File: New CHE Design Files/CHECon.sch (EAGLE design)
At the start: 42 parts, among them U2 MAX232SOIC16, U3 RS485SOIC

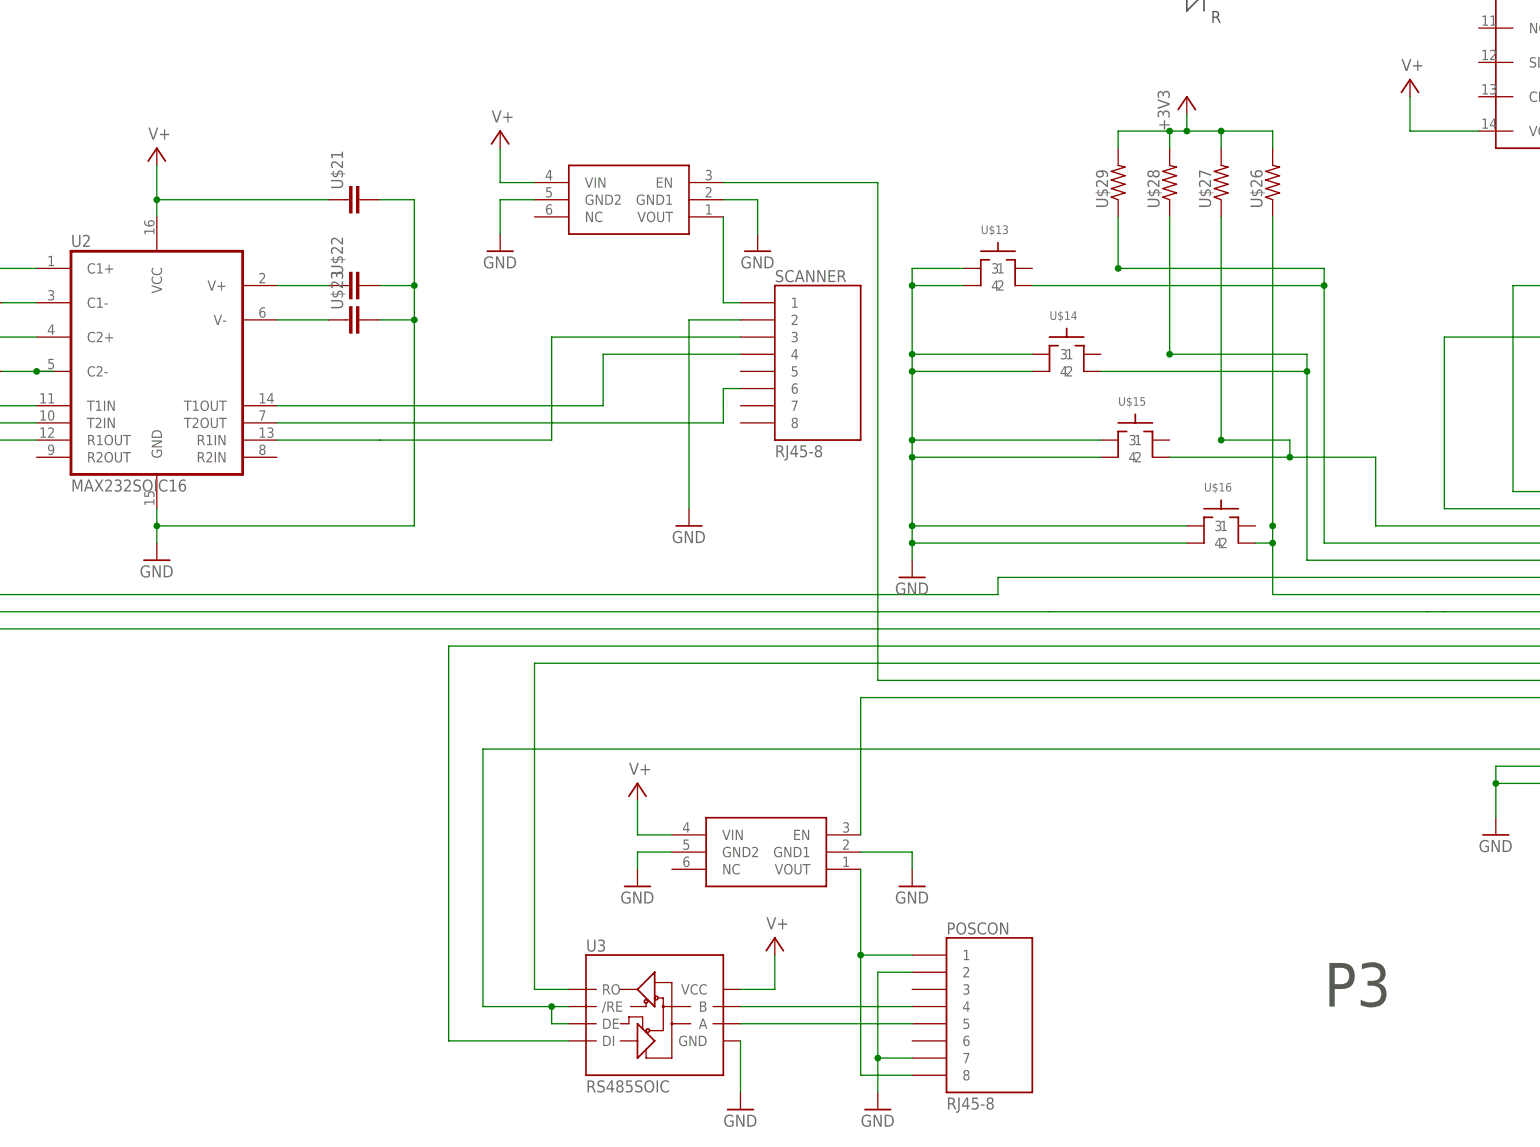
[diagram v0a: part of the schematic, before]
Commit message: P4
Fixed MAX232 rail, moved to 3.3V
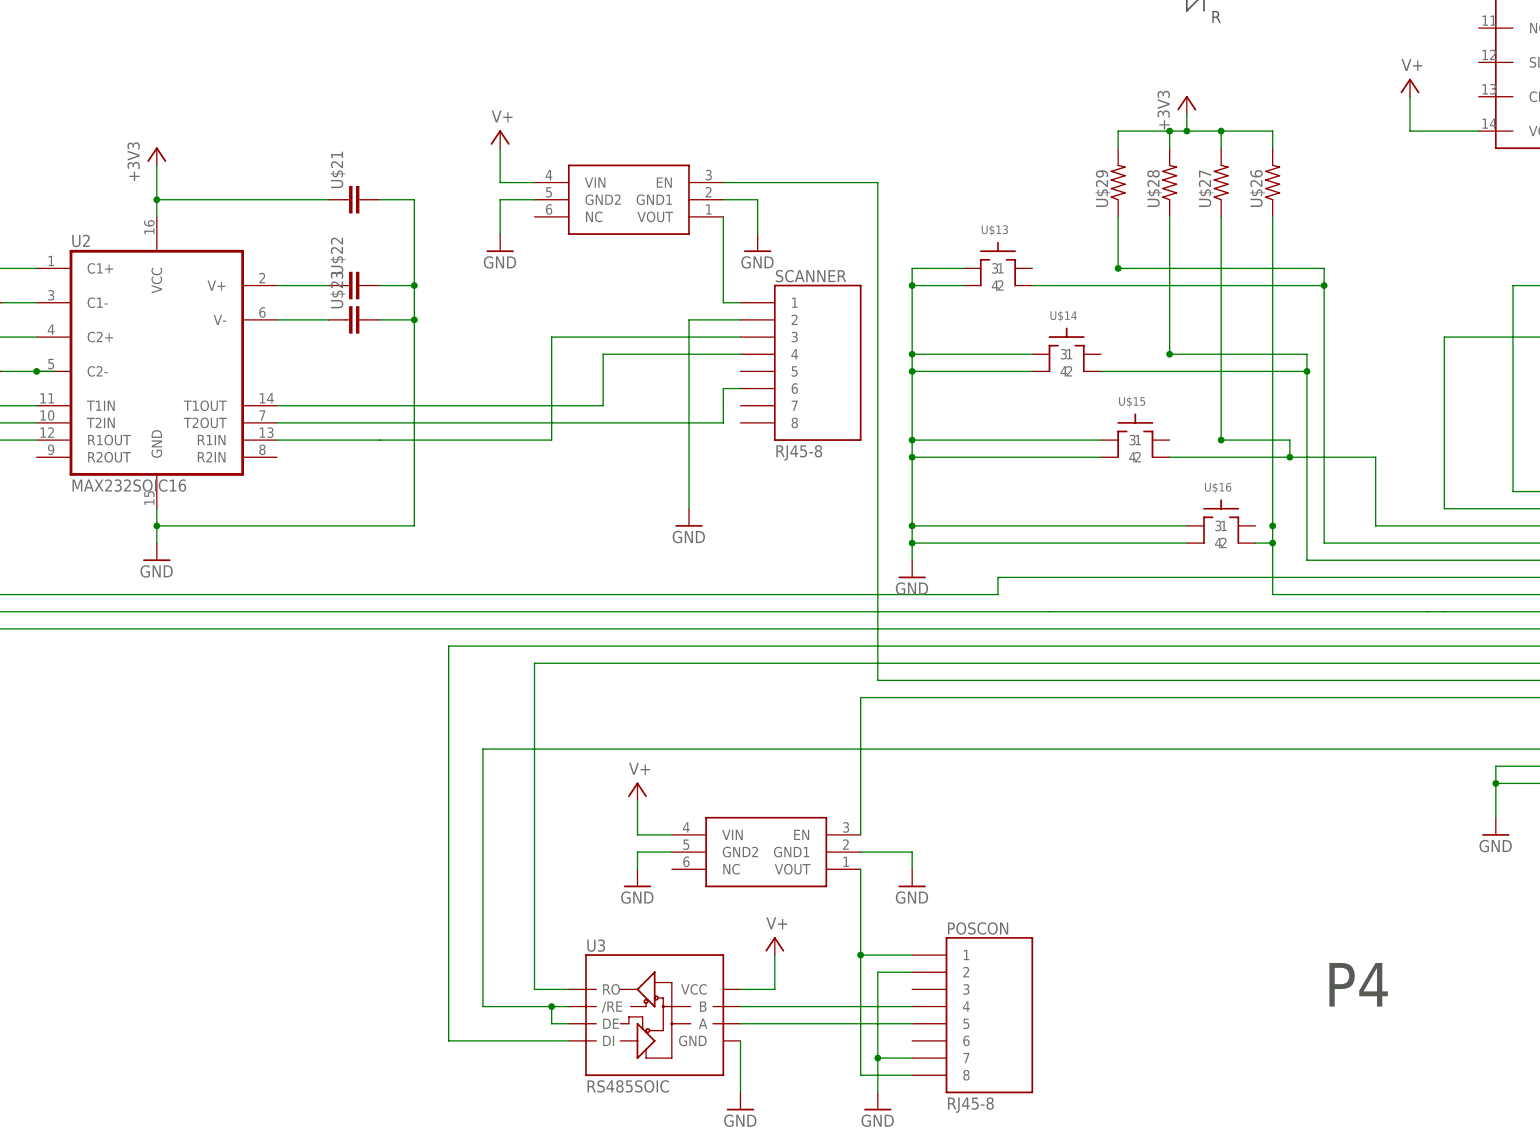
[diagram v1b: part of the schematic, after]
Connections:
- net +3V3: now also U$21.1, U2.VCC
- net V+: no longer U$21.1, U2.VCC
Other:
- note added: "P4"
- note removed: "P3"
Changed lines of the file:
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@@
 <part name="U$4" library="GW-devices" deviceset="MIC94061" device="C6"/>
 <part name="U$5" library="GW-devices" deviceset="MIC94061" device="C6"/>
-<part name="SUPPLY2" library="supply2" deviceset="V+" device=""/>
 <part name="SUPPLY4" library="supply2" deviceset="V+" device=""/>
 <part name="GND9" library="supply1" deviceset="GND" device=""/>
@@
 </part>
 <part name="U$37" library="SparkFun" deviceset="DIODE-ZENER" device="-BZT52"/>
+<part name="+3V2" library="supply1" deviceset="+3V3" device=""/>
 </parts>
 <sheets>
 <sheet>
 <plain>
-<text x="-233.68" y="60.96" size="6.4516" layer="97">P3</text>
+<text x="-233.68" y="60.96" size="6.4516" layer="97">P4</text>
 </plain>
 <instances>
@@
 <instance part="U$4" gate="G$1" x="-337.82" y="180.34" rot="R180"/>
 <instance part="U$5" gate="G$1" x="-317.5" y="83.82" rot="R180"/>
-<instance part="SUPPLY2" gate="1" x="-406.4" y="187.96"/>
 <instance part="SUPPLY4" gate="1" x="-335.28" y="93.98"/>
 <instance part="GND9" gate="1" x="-335.28" y="78.74"/>
@@
 </instance>
 <instance part="U$37" gate="G$1" x="-152.4" y="177.8" rot="R90"/>
+<instance part="+3V2" gate="G$1" x="-406.4" y="187.96"/>
 </instances>
 <busses>
@@
 <wire x1="-167.64" y1="182.88" x2="-167.64" y2="170.18" width="0.1524" layer="91"/>
 <junction x="-152.4" y="182.88"/>
+</segment>
+<segment>
+<wire x1="-406.4" y1="185.42" x2="-406.4" y2="180.34" width="0.1524" layer="91"/>
+<wire x1="-406.4" y1="180.34" x2="-406.4" y2="177.8" width="0.1524" layer="91"/>
+<wire x1="-381" y1="180.34" x2="-406.4" y2="180.34" width="0.1524" layer="91"/>
+<junction x="-406.4" y="180.34"/>
+<pinref part="U2" gate="G$1" pin="VCC"/>
+<pinref part="U$21" gate="G$1" pin="1"/>
+<pinref part="+3V2" gate="G$1" pin="+3V3"/>
 </segment>
 </net>
@@
 </segment>
 <segment>
-<wire x1="-406.4" y1="185.42" x2="-406.4" y2="180.34" width="0.1524" layer="91"/>
-<wire x1="-406.4" y1="180.34" x2="-406.4" y2="177.8" width="0.1524" layer="91"/>
-<wire x1="-381" y1="180.34" x2="-406.4" y2="180.34" width="0.1524" layer="91"/>
-<junction x="-406.4" y="180.34"/>
-<pinref part="U2" gate="G$1" pin="VCC"/>
-<pinref part="SUPPLY2" gate="1" pin="V+"/>
-<pinref part="U$21" gate="G$1" pin="1"/>
-</segment>
-<segment>

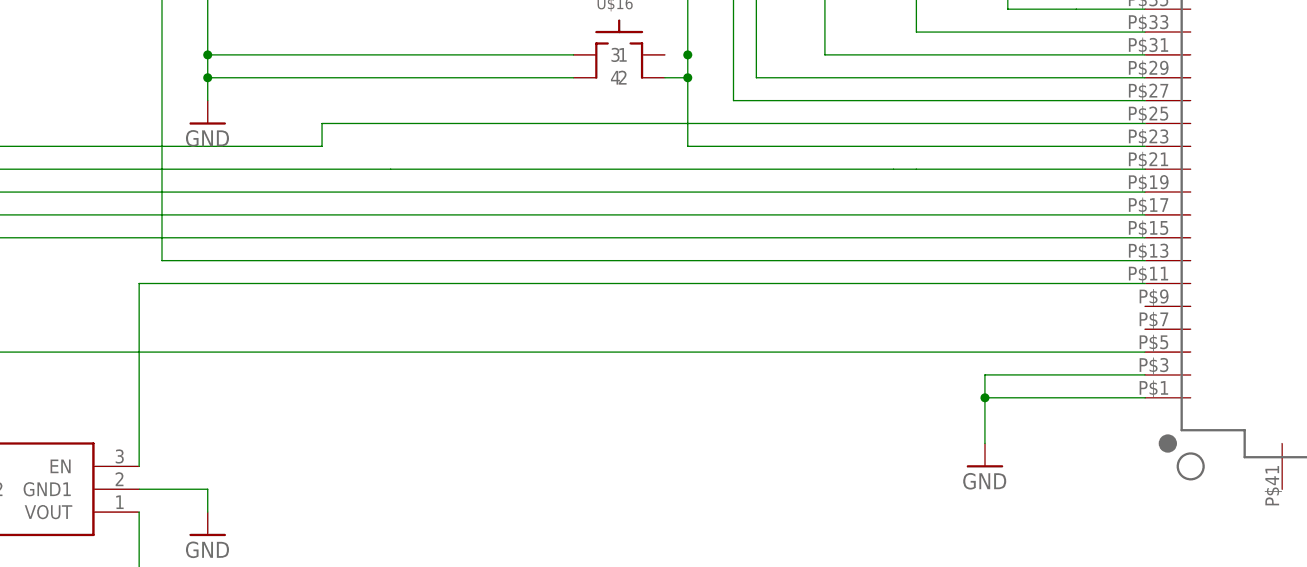
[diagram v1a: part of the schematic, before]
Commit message: P4 update
Moved scanner power select to PTD3 to avoid conflict with EEPROM CS
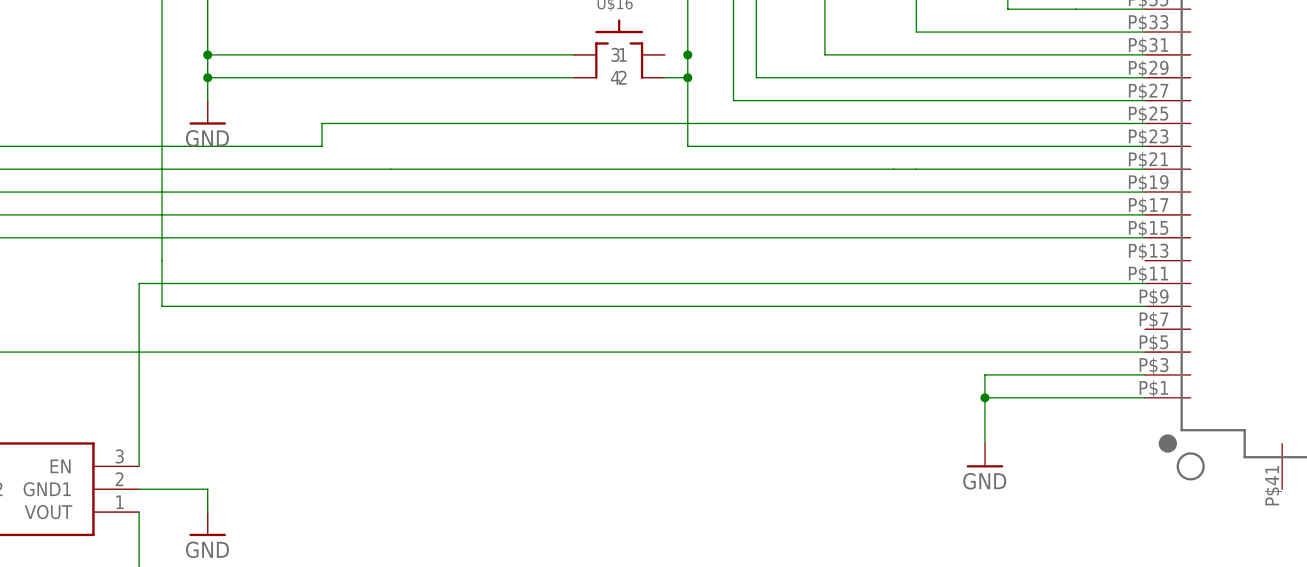
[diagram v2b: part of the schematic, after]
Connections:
- net N$40: now also U$10.PTD3/SPI0_SIN/UART2_TX/I2C0_SCL/GPIO5_BSM_CLK; no longer U$10.PTD5/ADC0_SE6B/SPI0_PCS2/!UART0_CTS!/!UART0_COL!/FTM0_CH5/!EWM_OUT
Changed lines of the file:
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@@
 <wire x1="-322.58" y1="182.88" x2="-299.72" y2="182.88" width="0.1524" layer="91"/>
 <wire x1="-299.72" y1="182.88" x2="-299.72" y2="109.22" width="0.1524" layer="91"/>
-<pinref part="U$10" gate="G$1" pin="PTD5/ADC0_SE6B/SPI0_PCS2/!UART0_CTS!/!UART0_COL!/FTM0_CH5/!EWM_OUT"/>
-<wire x1="-299.72" y1="109.22" x2="-190.5" y2="109.22" width="0.1524" layer="91"/>
+<pinref part="U$10" gate="G$1" pin="PTD3/SPI0_SIN/UART2_TX/I2C0_SCL/GPIO5_BSM_CLK"/>
+<wire x1="-190.5" y1="104.14" x2="-299.72" y2="104.14" width="0.1524" layer="91"/>
+<wire x1="-299.72" y1="104.14" x2="-299.72" y2="109.22" width="0.1524" layer="91"/>
 </segment>
 </net>
